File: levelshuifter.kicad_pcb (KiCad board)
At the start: 2 copper layers, 56 x 111 mm, 25 parts, among them J1 Screw_Terminal_01x02, J2 Conn_02x20_Odd_Even, J3 Conn_02x08_Odd_Even, J4 Conn_02x08_Odd_Even, J5 Conn_02x08_Odd_Even, U1 LM1117-3.3, U2 74LVC8T245PW, U3 74LVC8T245PW, U4 74LVC8T245PW, U5 L7805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

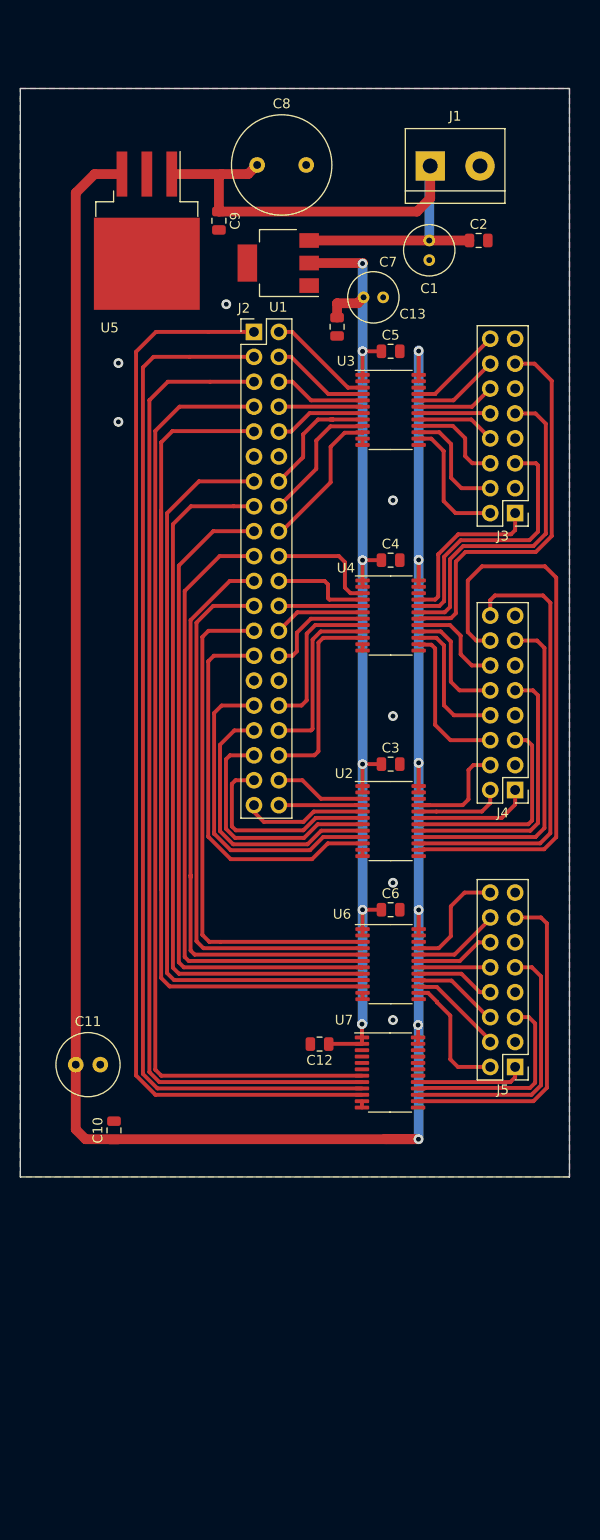
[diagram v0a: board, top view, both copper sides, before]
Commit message: cambio de membrete
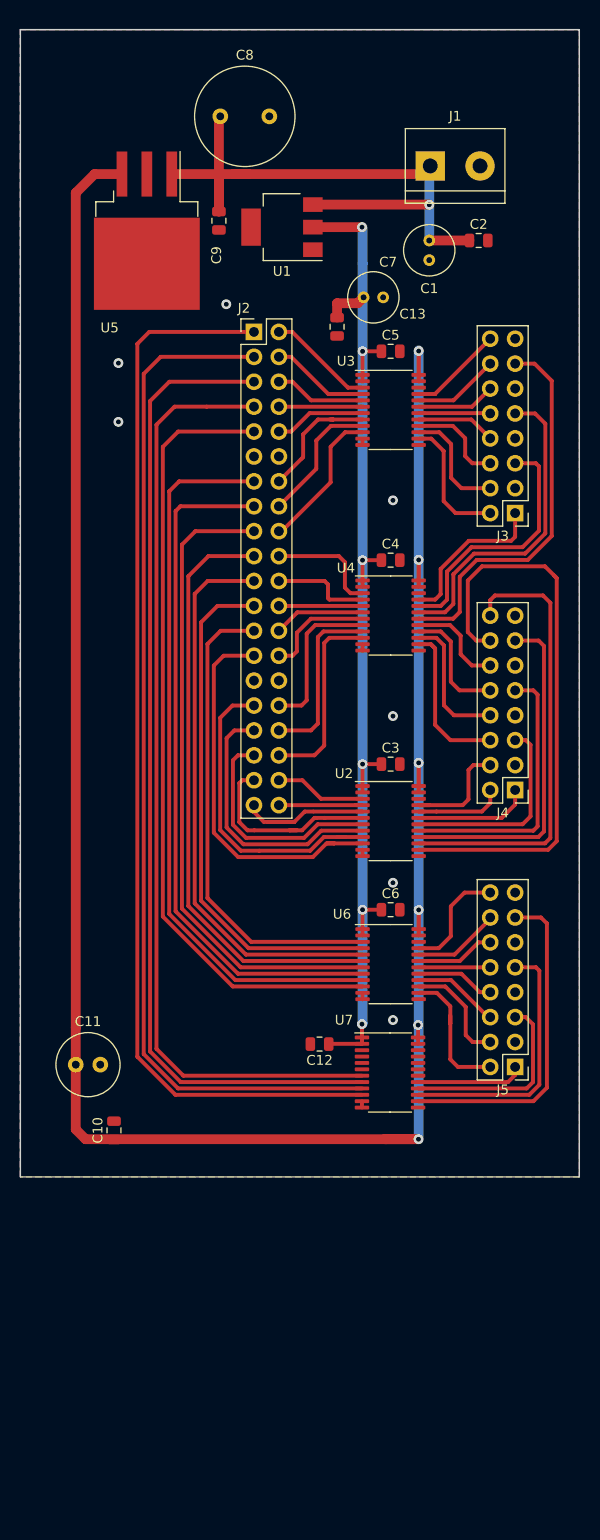
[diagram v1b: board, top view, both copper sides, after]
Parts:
- moved C8 6.22 mm to (75.4, 37.8)
- moved U1 3.68 mm to (81.7, 49.1)
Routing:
- net /A4_8: track 124.1 -> 81.2 mm
- net /A4_1: track 52.5 -> 48.9 mm
- net /A4_2: track 56.3 -> 53.0 mm
- net +3V3: track 124.5 -> 127.6 mm
- net /A4_6: track 73.8 -> 70.7 mm
- net /A4_4: track 64.2 -> 61.3 mm
- net /A4_5: track 68.7 -> 65.9 mm
- net +12V: track 62.8 -> 65.5 mm, vias 0 -> 1
- net /A4_7: track 77.3 -> 74.7 mm
- net /A3_3: track 12.6 -> 15.3 mm
- net /A4_3: track 59.7 -> 57.4 mm
- net Net-(J5-Pad4): track 9.74 -> 11.5 mm
- net /A5_7: track 106.8 -> 105.0 mm
- net /A3_5: track 25.0 -> 23.3 mm
- net /A5_6: track 102.1 -> 100.6 mm
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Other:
- board size 56 x 111 mm -> 57 x 117 mm

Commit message: segundos cambios
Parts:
- added FID1: Fiducial, Fiducial:Fiducial_1mm_Mask2mm, F.Cu at (60.0, 42.0)
- added FID2: Fiducial, Fiducial:Fiducial_1mm_Mask2mm, F.Cu at (102.0, 124.8)
- added H1: MountingHole, MountingHole:MountingHole_3mm, F.Cu at (104.2, 33.0)
- added H3: MountingHole, MountingHole:MountingHole_3mm, F.Cu at (66.0, 176.2)
- added H4: MountingHole, MountingHole:MountingHole_3mm, F.Cu at (104.2, 176.2)
- C10: value 1uF -> 4.7uF
- moved C13 24.8 mm to (81.5, 35.1), turned to 180 degrees
- moved J5 24.2 mm to (105.5, 159.0)
- moved U7 24.2 mm to (92.7, 159.6)
- moved C12 21.2 mm to (92.8, 152.3), turned to 0 degrees
- moved C7 18.6 mm to (82.5, 39.3), turned to 180 degrees
- moved C2 13.2 mm to (89.8, 44.7), turned to 270 degrees
- moved C5 12.6 mm to (92.8, 49.2)
- moved J3 12.1 mm to (105.5, 66.2)
- moved U3 11.9 mm to (92.8, 55.9)
- moved J1 10.1 mm to (95.0, 33.0), turned to 180 degrees
- moved U6 9.33 mm to (92.8, 133.6)
- moved C6 8.75 mm to (92.8, 127.5)
- moved C1 7.40 mm to (93.5, 43.9), turned to 0 degrees
- moved C4 7.40 mm to (92.8, 75.7)
- moved U4 6.95 mm to (92.8, 81.8)
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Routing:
- net +5V: track 233.2 -> 290.5 mm
- net +3V3: track 127.6 -> 163.1 mm
- net /A5_6: track 100.6 -> 130.5 mm
- net /A5_5: track 96.4 -> 123.8 mm
- net /A5_7: track 105.0 -> 132.1 mm
- net /A5_8: track 109.6 -> 135.4 mm
- net Net-(J5-Pad6): track 8.86 -> 25.2 mm
- net Net-(J5-Pad4): track 11.5 -> 27.1 mm
- net Net-(J5-Pad8): track 8.08 -> 23.4 mm
- net Net-(J5-Pad2): track 14.4 -> 29.7 mm
- net /A4_1: track 48.9 -> 63.7 mm
- net Net-(J4-Pad12): track 10.1 -> 24.9 mm
- net /A1_8: track 14.8 -> 28.8 mm
- net Net-(J5-Pad10): track 7.30 -> 21.1 mm
- net /A4_2: track 53.0 -> 66.4 mm
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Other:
- board size 57 x 117 mm -> 55 x 153 mm
